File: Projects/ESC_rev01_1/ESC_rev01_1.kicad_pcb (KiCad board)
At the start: 4 copper layers, 100 x 75 mm, 178 parts, among them J1 XT30PW-M, J10 Conn_01x04_2mnt, J11 TYPE-C-31-M-12, J2 XH-2PWBPZ, J3 XH-2PWBPZ, J4 Conn_01x06, J5 Conn_01x03, J6 Conn_01x01, J7 Conn_01x01, J8 Conn_01x01, J9 Conn_01x04_2mnt, Q1 HSBA15810C, Q2 HSBA15810C, Q3 HSBA15810C, Q4 HSBA15810C, Q5 HSBA15810C, Q6 HSBA15810C, SW1 PTS526SK15SMTR2LFS, U1 AMS1117-3.3, U2 STM32F405RGTx, U3 DRV8302DCA, U4 ESDCAN24-2BLY, U5 744227S, U6 SN65HVD230, Y1 8M 10ppm X50328MSB2GI

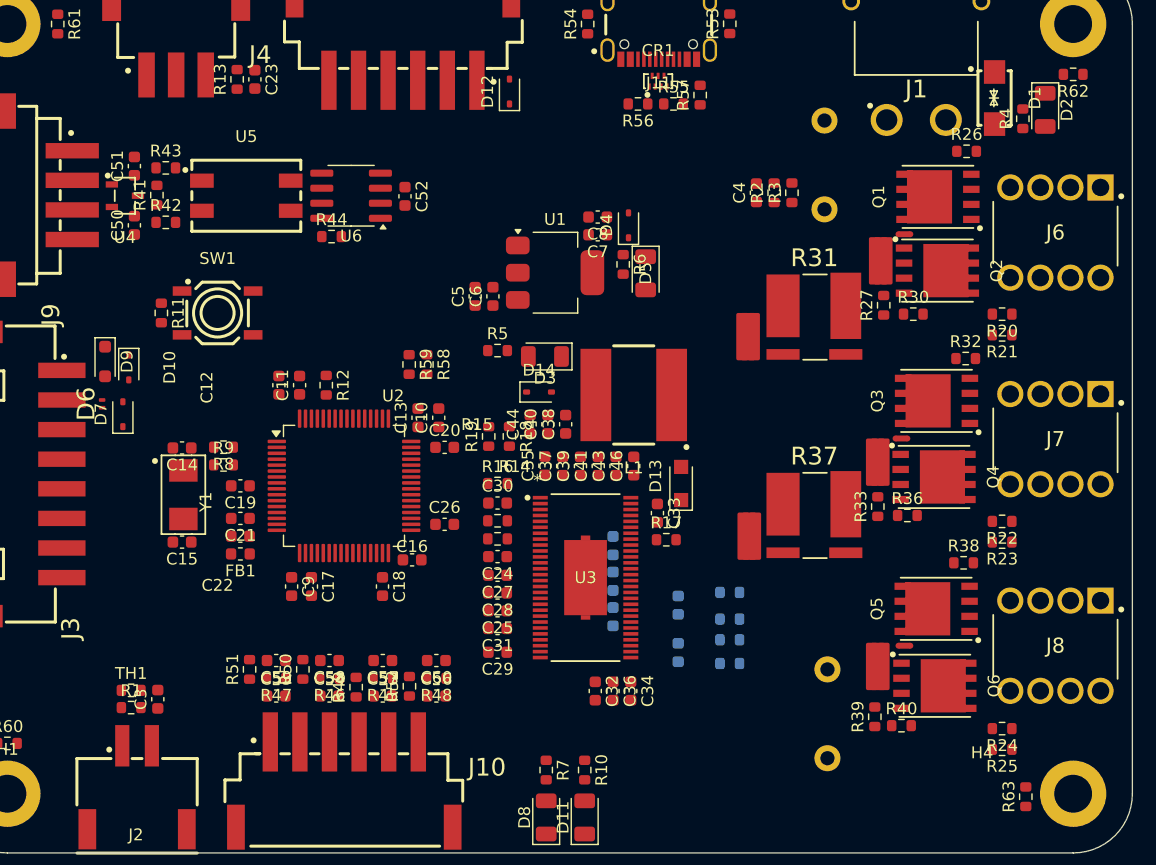
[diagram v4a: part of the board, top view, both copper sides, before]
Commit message: Update 11
Draft routing - diff signals and power
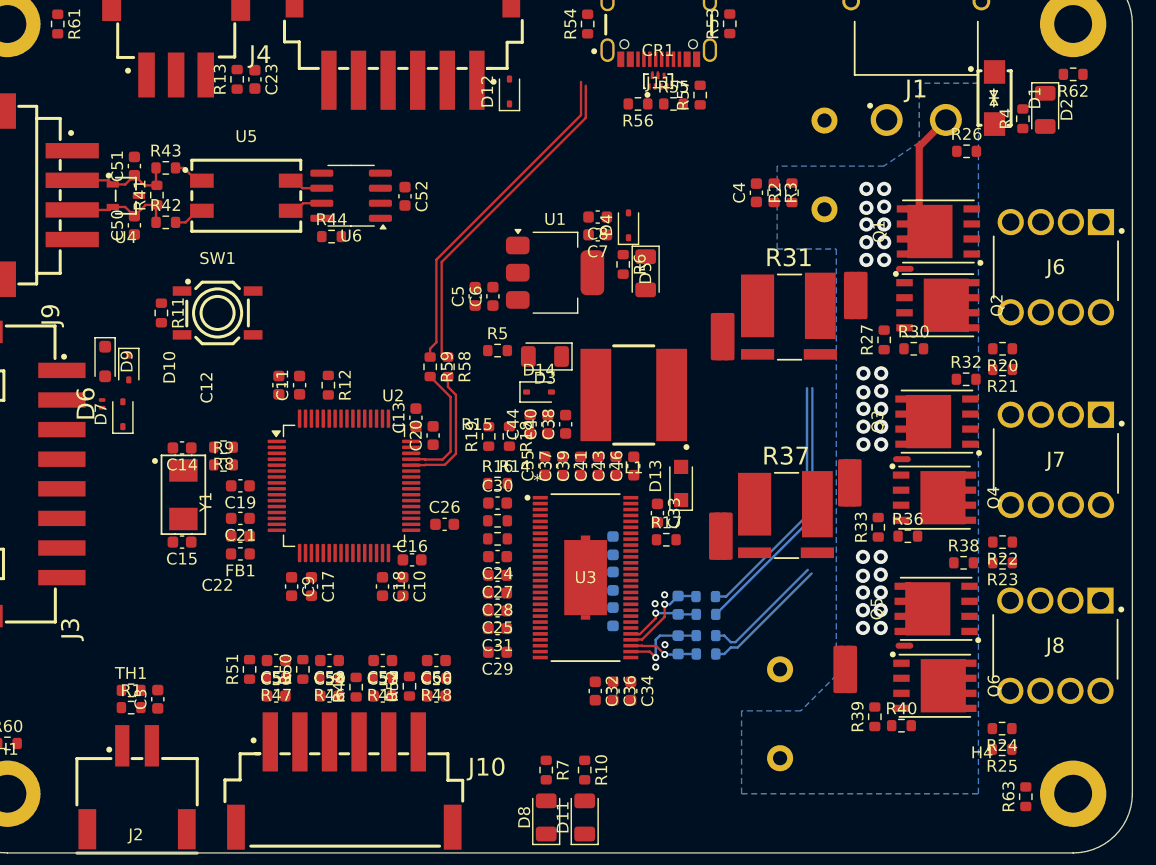
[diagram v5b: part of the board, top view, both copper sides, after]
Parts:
- moved C10 14.6 mm to (213.4, 157.5), turned to -90 degrees
- moved C2 4.00 mm to (245.2, 168.2), turned to 90 degrees
- moved NT2 3.61 mm to (251.6, 132.9)
- moved NT5 2.94 mm to (251.1, 148.8)
- moved Q2 2.93 mm to (258.6, 133.8)
- moved NT1 2.93 mm to (255.8, 130.7)
- moved R20 2.93 mm to (264.0, 137.4)
- moved R21 2.93 mm to (264.0, 139.2)
- moved R27 2.93 mm to (254.0, 136.7)
- moved R30 2.93 mm to (256.5, 137.4)
- moved Q1 2.93 mm to (258.6, 127.5)
- moved J6 2.93 mm to (272.3, 126.7)
- moved NT8 2.76 mm to (250.8, 164.5)
- moved NT6 2.40 mm to (240.2, 153.2)
- moved R37 2.40 mm to (245.8, 151.5)
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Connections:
- net Net-(R42-Pad2) renamed /[07] - CAN/R_CAN_P
- net Net-(R43-Pad2) renamed /[07] - CAN/R_CAN_N
- R58 pad 2: /[09] - USB/USB_N -> USB_DN
- R59 pad 2: /[09] - USB/USB_P -> USB_DP
- U2 pad 44: /[04] - MCU/USB_DM -> USB_DN
- U2 pad 45: /[04] - MCU/USB_DP -> USB_DP
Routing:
- net /[09] - USB/USB-C_P: track 0.00 -> 28.8 mm
- net /[09] - USB/USB-C_N: track 0.00 -> 28.8 mm
- net /[06] - MOSFETs/SH1_N: track 0.00 -> 22.5 mm
- net /[06] - MOSFETs/SH1_P: track 0.00 -> 21.3 mm
- net +VDC: track 0.00 -> 13.0 mm, vias 0 -> 30
- net USB_DN: track 0.00 -> 11.0 mm
- net /[06] - MOSFETs/SH2_N: track 0.00 -> 10.9 mm
- net USB_DP: track 0.00 -> 10.7 mm
- net /[06] - MOSFETs/SH2_P: track 0.00 -> 10.5 mm
- net /[07] - CAN/C_CAN_P: track 0.00 -> 9.47 mm
- net /[07] - CAN/C_CAN_N: track 0.00 -> 9.47 mm
- net S1_P: track 0.00 -> 7.68 mm, vias 0 -> 1
- net S2_P: track 0.00 -> 7.38 mm, vias 0 -> 1
- net S1_N: track 0.00 -> 6.57 mm, vias 0 -> 1
- net S2_N: track 0.00 -> 5.86 mm, vias 0 -> 1
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- added copper zone on B.Cu, net +VDC

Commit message: Update 12
Continue routing
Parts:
- added NT9: NetTie_2, NetTie:NetTie-2_SMD_Pad0.5mm, F.Cu at (226.5, 159.8)
- C26, C30, C31, R14: moved to B.Cu
- moved R25 48.7 mm to (265.1, 122.6), turned to 90 degrees
- moved R24 47.0 mm to (266.8, 122.6), turned to -90 degrees
- moved R20 32.8 mm to (265.8, 170.2), turned to 90 degrees
- moved R21 31.1 mm to (264.1, 170.2), turned to -90 degrees
- moved NT1 14.3 mm to (268.0, 123.2), turned to -90 degrees
- moved C17 14.1 mm to (201.6, 143.9), turned to 180 degrees
- moved C26 13.7 mm to (230.4, 149.8), turned to -90 degrees
- moved NT7 13.5 mm to (267.2, 169.6), turned to 90 degrees
- moved R14 7.80 mm to (228.9, 149.8), turned to 90 degrees
- moved NT4 7.14 mm to (259.0, 153.0), turned to 180 degrees
- moved C31 6.45 mm to (225.0, 155.7), turned to -90 degrees
- moved C30 6.04 mm to (227.4, 149.8), turned to 90 degrees
- moved R19 5.92 mm to (220.6, 150.7), turned to 180 degrees
- moved R18 4.77 mm to (220.6, 149.2), turned to 0 degrees
- moved C38 3.28 mm to (224.1, 142.7), turned to -90 degrees
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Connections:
- net Net-(U3-CP1) renamed /[05] - MOSFET DRIVER/CP1
- net Net-(U3-CP2) renamed /[05] - MOSFET DRIVER/CP2
- net Net-(U3-DTC) renamed /[05] - MOSFET DRIVER/DTC
- C24 pad 1: /[05] - MOSFET DRIVER/DVDD -> /[05] - MOSFET DRIVER/OC_ADJ
- C27 pad 1: /[05] - MOSFET DRIVER/DVDD -> /[05] - MOSFET DRIVER/OC_ADJ
- CR1 pad 6: /[09] - USB/USB-C_N -> /[09] - USB/USB-C_P
- CR1 pad 7: /[09] - USB/USB-C_P -> /[09] - USB/USB-C_N
- U2 pad 1: unconnected-(U2-VBAT-Pad1) -> +3V3
- U2 pad 52: /[04] - MCU/HALL_3 -> HALL_3_OUT
- U2 pad 58: /[04] - MCU/HALL_1 -> HALL_1_OUT
- U2 pad 59: /[04] - MCU/HALL_2 -> HALL_2_OUT
- U3 pad 11: /[05] - MOSFET DRIVER/DVDD -> /[05] - MOSFET DRIVER/OC_ADJ
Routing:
- net GND: track 0.00 -> 77.5 mm, vias 4 -> 38
- net /[04] - MCU/NRST: track 0.00 -> 43.3 mm
- net +3V3: track 0.00 -> 40.2 mm, vias 0 -> 1
- net /[04] - MCU/SWDIO: track 0.00 -> 37.0 mm
- net /[04] - MCU/RX_SCL_MOSI: track 0.00 -> 36.9 mm, vias 0 -> 2
- net /[04] - MCU/TX_SDA_NSS: track 0.00 -> 36.2 mm, vias 0 -> 3
- net /[04] - MCU/SERVO: track 0.00 -> 34.9 mm, vias 0 -> 2
- net /[04] - MCU/SCK_ADC_EXT: track 0.00 -> 34.7 mm, vias 0 -> 2
- net /[04] - MCU/MISO_ADC_EXT2: track 0.00 -> 32.5 mm, vias 0 -> 2
- net /[04] - MCU/SWCLK: track 0.00 -> 32.0 mm
- net /[04] - MCU/LED_RED: track 0.00 -> 31.6 mm, vias 0 -> 2
- net /[04] - MCU/LED_GREEN: track 0.00 -> 30.5 mm, vias 0 -> 2
- net CAN_RX: track 0.00 -> 28.1 mm
- net HALL_3_OUT: track 0.00 -> 27.0 mm, vias 0 -> 2
- net +5V: track 0.00 -> 26.0 mm
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- added copper zone on F.Cu, net +VDC
- added copper zone on F.Cu, net /[06] - MOSFETs/PHASE_1
- added copper zone on In1.Cu, net GND
- added copper zone on In2.Cu, net GND

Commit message: Update 01
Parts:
- C1, C2: footprint DF_ESC_rev01_1:CAP-TH_BD16.0-P7.50-D1.2-FD -> KeIr_lib:CAPPRD750W80D1600H2500
- C31: value 2u2 -> 22n
- CR1: footprint DF_ESC_rev01_1:XSON-7_L2.2-W1.2-P0.50-BL -> KeIr_lib:XSON-7_L2.2-W1.2-P0.50-BL; moved to B.Cu
- D1: footprint DF_ESC_rev01_1:SMA_L4.4-W2.8-LS5.1-BI -> KeIr_lib:SMA_L4.4-W2.8-LS5.1-BI
- D6: footprint DF_ESC_rev01_1:D_SOD-882_BI -> KeIr_lib:D_SOD-882_BI
- J1: footprint DF_ESC_rev01_1:CONN-TH_XT30PW-M -> KeIr_lib:CONN-TH_XT30PW-M
- J10: value Conn_01x04_2mnt -> Conn_01x06_2mnt; footprint DF_ESC_rev01_1:CONN-SMD_6P-P2.50_DEALON_XH-6PWB -> KeIr_lib:CONN_DEALON_XH-6PWB
- J11: footprint DF_ESC_rev01_1:USB-C_SMD-TYPE-C-31-M-12_1 -> KeIr_lib:USB-C_SMD-TYPE-C-31-M-12_1
- J2: footprint DF_ESC_rev01_1:CONN-SMD_XH-2PWBPZ -> KeIr_lib:CONN-SMD_XH-2PWBPZ
- J3: footprint DF_ESC_rev01_1:CONN-SMD_8P-P2.50_HX25003-8AWB -> KeIr_lib:CONN-SMD_8P-P2.50_HX25003-8AWB
- J4: value Conn_01x06 -> Conn_01x06_2mnt; footprint DF_ESC_rev01_1:CONN-SMD_6P-P2.50_DEALON_XH-6PWB -> KeIr_lib:CONN_DEALON_XH-6PWB
- J5: footprint DF_ESC_rev01_1:CONN-SMD_XH-3AWB -> KeIr_lib:CONN-SMD_XH-3AWB
- J6, J7, J8: footprint DF_ESC_rev01_1:WE_7461084 -> KeIr_lib:WE_7461084
- J9: footprint DF_ESC_rev01_1:CONN-SMD_S4B-XH-SM4-TB-LF-SN -> KeIr_lib:CONN-SMD_S4B-XH-SM4-TB-LF-SN
- L1: footprint DF_ESC_rev01_1:IND-SMD_L7.8-W7.8_SDR0805 -> KeIr_lib:IND-SMD_L7.8-W7.8_SDR0805
- NT2, NT5, NT8: footprint DF_ESC_rev01_1:NetTie-2_SMD_Pad_4.0x2.0mm -> NetTie:NetTie-2_SMD_Pad0.5mm
- NT3, NT6: footprint DF_ESC_rev01_1:NetTie-2_SMD_Pad_4.0x2.0mm -> KeIr_lib:NetTie-2_SMD_Pad_4.0x2.0mm
- NT4, NT7, NT9: footprint NetTie:NetTie-2_SMD_Pad0.5mm -> KeIr_lib:NetTie-2_SMD_Pad_4.0x2.0mm
- Q1, Q2, Q3, Q4, Q5, Q6: footprint DF_ESC_rev01_1:PQFN-8_L6.0-W5.0-P1.27-LS6.0-BL -> KeIr_lib:PQFN-8_L6.0-W5.0-P1.27-LS6.0-BL
- R12: value 100R -> 100k
- R31, R37: footprint DF_ESC_rev01_1:RES_VISHAY_WSLP27261L000 -> KeIr_lib:RES_VISHAY_WSLP27261L000
- R7: value 1k -> 0R
- R9: value 0R -> 1k
- SW1: footprint DF_ESC_rev01_1:SW-SMD_4P-L5.2-W5.2-P3.70-LS6.4 -> KeIr_lib:SW-SMD_4P-L5.2-W5.2-P3.70-LS6.4
- U3: footprint DF_ESC_rev01_1:DCA56_6P35X3P61 -> KeIr_lib:DCA56_6P35X3P61
- U4: footprint DF_ESC_rev01_1:SOT-23-3_L3.0-W1.7-P0.95-LS2.9-BR -> KeIr_lib:SOT-23-3_L3.0-W1.7-P0.95-LS2.9-BR
- U5: footprint DF_ESC_rev01_1:FILTER-SMD_4P-L9.2-W6.0-P2.54-TL -> KeIr_lib:FILTER-SMD_4P-L9.2-W6.0-P2.54-TL
- Y1: footprint DF_ESC_rev01_1:CRYSTAL-SMD_L5.0-W3.2 -> KeIr_lib:CRYSTAL-SMD_L5.0-W3.2
- moved C5 19.2 mm to (236.6, 123.1), turned to 0 degrees
- moved C6 17.2 mm to (236.6, 124.6), turned to 0 degrees
- moved D5 13.7 mm to (220.8, 133.8), turned to 0 degrees
- moved R58 9.46 mm to (216.8, 148.4), turned to 180 degrees
- moved D4 9.23 mm to (224.2, 130.0)
- moved R6 9.06 mm to (224.0, 133.4)
- moved R59 7.93 mm to (216.8, 146.8), turned to 180 degrees
- moved C8 6.33 mm to (226.8, 130.7), turned to 0 degrees
- moved R56 6.16 mm to (228.4, 114.2), turned to 90 degrees
- moved U1 5.66 mm to (230.4, 126.0), turned to 180 degrees
- moved D11 4.65 mm to (224.1, 177.1)
- moved R10 4.65 mm to (224.1, 173.1)
- moved D3 4.57 mm to (220.8, 136.9), turned to 0 degrees
- moved NT7 4.40 mm to (262.8, 169.8)
- moved NT4 4.34 mm to (263.2, 154.1), turned to 90 degrees
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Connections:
- J10 pad 1: GND -> +5V
- J10 pad 2: /[08] - FILTERS/HALL_3_IN -> /[08] - FILTERS/TEMP_IN
- J10 pad 3: /[08] - FILTERS/HALL_2_IN -> /[08] - FILTERS/HALL_1_IN
- J10 pad 4: /[08] - FILTERS/HALL_1_IN -> /[08] - FILTERS/HALL_2_IN
- J10 pad 5: /[08] - FILTERS/TEMP_IN -> /[08] - FILTERS/HALL_3_IN
- J10 pad 6: +5V -> GND
- NT1 pad 1: H1_VS -> /[05] - MOSFET DRIVER/DVDD
- NT1 pad 2: /[06] - MOSFETs/PHASE_1 -> /[05] - MOSFET DRIVER/OC_ADJ
- NT2 pad 1: /[06] - MOSFETs/SH1_N -> H1_VS
- NT2 pad 2: H1_LOW -> /[06] - MOSFETs/PHASE_1
- NT3 pad 1: GND -> /[06] - MOSFETs/SH1_N
- NT3 pad 2: /[06] - MOSFETs/SH1_P -> H1_LOW
- NT4 pad 1: H2_VS -> GND
- NT4 pad 2: /[06] - MOSFETs/PHASE_2 -> /[06] - MOSFETs/SH1_P
- NT5 pad 1: /[06] - MOSFETs/SH2_N -> H2_VS
- NT5 pad 2: H2_LOW -> /[06] - MOSFETs/PHASE_2
- NT6 pad 1: GND -> /[06] - MOSFETs/SH2_N
- NT6 pad 2: /[06] - MOSFETs/SH2_P -> H2_LOW
- NT7 pad 1: H3_VS -> GND
- NT7 pad 2: /[06] - MOSFETs/PHASE_3 -> /[06] - MOSFETs/SH2_P
- NT8 pad 1: GND -> H3_VS
- NT8 pad 2: H3_LOW -> /[06] - MOSFETs/PHASE_3
- NT9 pad 1: /[05] - MOSFET DRIVER/DVDD -> GND
- NT9 pad 2: /[05] - MOSFET DRIVER/OC_ADJ -> H3_LOW
- R1 pad 1: ADC_TEMP -> GND
- R1 pad 2: +3V3 -> ADC_TEMP
- R7 pad 1: /[04] - MCU/LED_GREEN -> /[04] - MCU/PH_0_P
- R7 pad 2: Net-(D8-A) -> /[04] - MCU/PH_0
- R8 pad 1: /[04] - MCU/PH_0_P -> /[04] - MCU/PH_1
- R8 pad 2: /[04] - MCU/PH_0 -> /[04] - MCU/PH_1_P
- R9 pad 1: /[04] - MCU/PH_1 -> /[04] - MCU/LED_GREEN
- R9 pad 2: /[04] - MCU/PH_1_P -> Net-(D8-A)
- TH1 pad 1: ADC_TEMP -> +3V3
- TH1 pad 2: GND -> ADC_TEMP
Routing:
- net SENS2: track 2.43 -> 114.3 mm, vias 0 -> 2
- net SENS3: track 0.00 -> 111.1 mm, vias 0 -> 2
- net +3V3: track 40.2 -> 150.2 mm, vias 1 -> 12
- net SENS1: track 1.75 -> 92.2 mm, vias 0 -> 2
- net GND: track 77.5 -> 166.3 mm, vias 38 -> 87
- net H1_VS: track 2.74 -> 76.7 mm, vias 1 -> 2
- net +5V: track 26.0 -> 96.9 mm, vias 0 -> 5
- net H2_VS: track 6.58 -> 73.3 mm, vias 1 -> 2
- net AN_IN: track 3.72 -> 63.6 mm, vias 0 -> 2
- net M_H1: track 5.47 -> 55.2 mm, vias 0 -> 2
- net H3_VS: track 2.86 -> 51.8 mm, vias 1 -> 2
- net HALL_1_OUT: track 0.00 -> 40.0 mm, vias 0 -> 3
- net M_H2: track 5.16 -> 43.5 mm, vias 0 -> 2
- net H1_LOW: track 12.3 -> 45.8 mm
- net TEMP_MOTOR: track 0.00 -> 33.3 mm, vias 0 -> 2
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- added copper zone on F.Cu, net +5V
- added copper zone on F.Cu, net /[05] - MOSFET DRIVER/+5V_DRV
- added copper zone on F.Cu, net /[06] - MOSFETs/PHASE_2
- added copper zone on F.Cu, net /[06] - MOSFETs/PHASE_3
